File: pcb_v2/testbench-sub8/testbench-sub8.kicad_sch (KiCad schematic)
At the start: 25 parts, among them J3 conn, U1 74LS574, U2 74LS574, U3 74LS240, U4 74LS125, U5 74LS125, U6 74LS125, U7 74LS125

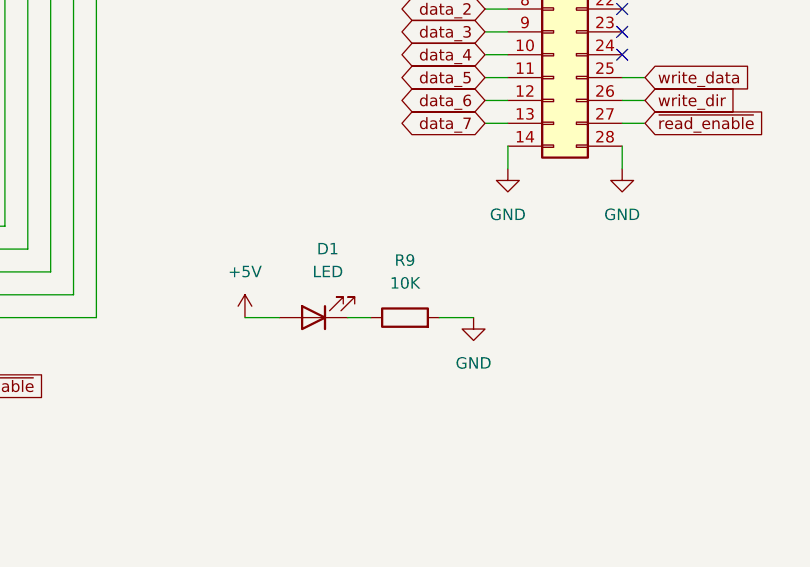
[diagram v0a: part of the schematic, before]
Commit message: correção no valor do resitor do led de power
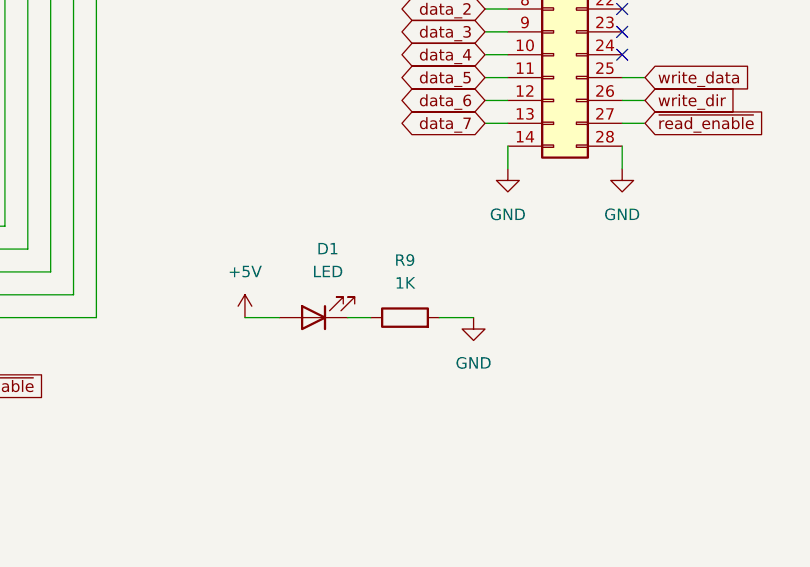
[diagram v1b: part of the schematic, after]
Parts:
- R9: value 10K -> 1K
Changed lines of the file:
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@@
 			)
 		)
-		(property "Value" "10K"
+		(property "Value" "1K"
 			(at 186.69 199.39 90)
 			(effects
